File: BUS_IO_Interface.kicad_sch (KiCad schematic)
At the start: 21 parts, among them U13 AS1016204-0108X0PWAY, U28 MAX31331TETB+, U88 TCAN1044ADDFRQ1, Y26 32.768kHz

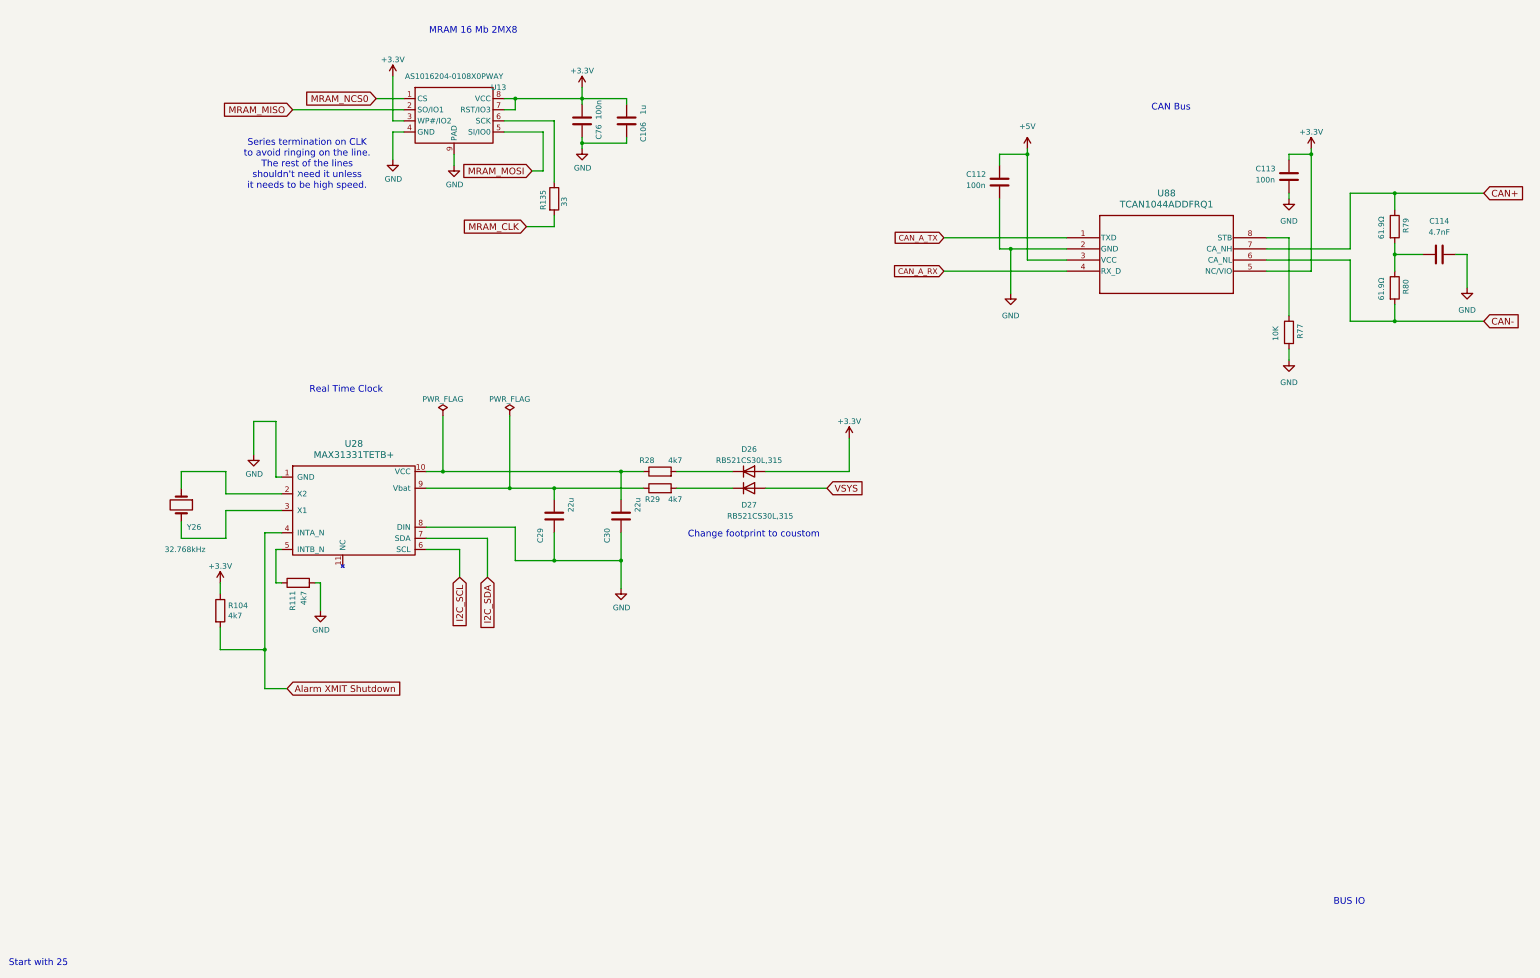
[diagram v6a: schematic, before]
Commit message: Re-annotate all parts
And get rid of the per-sheet annotation remarks.

Signed-off-by: Corey Minyard <corey@minyard.net>
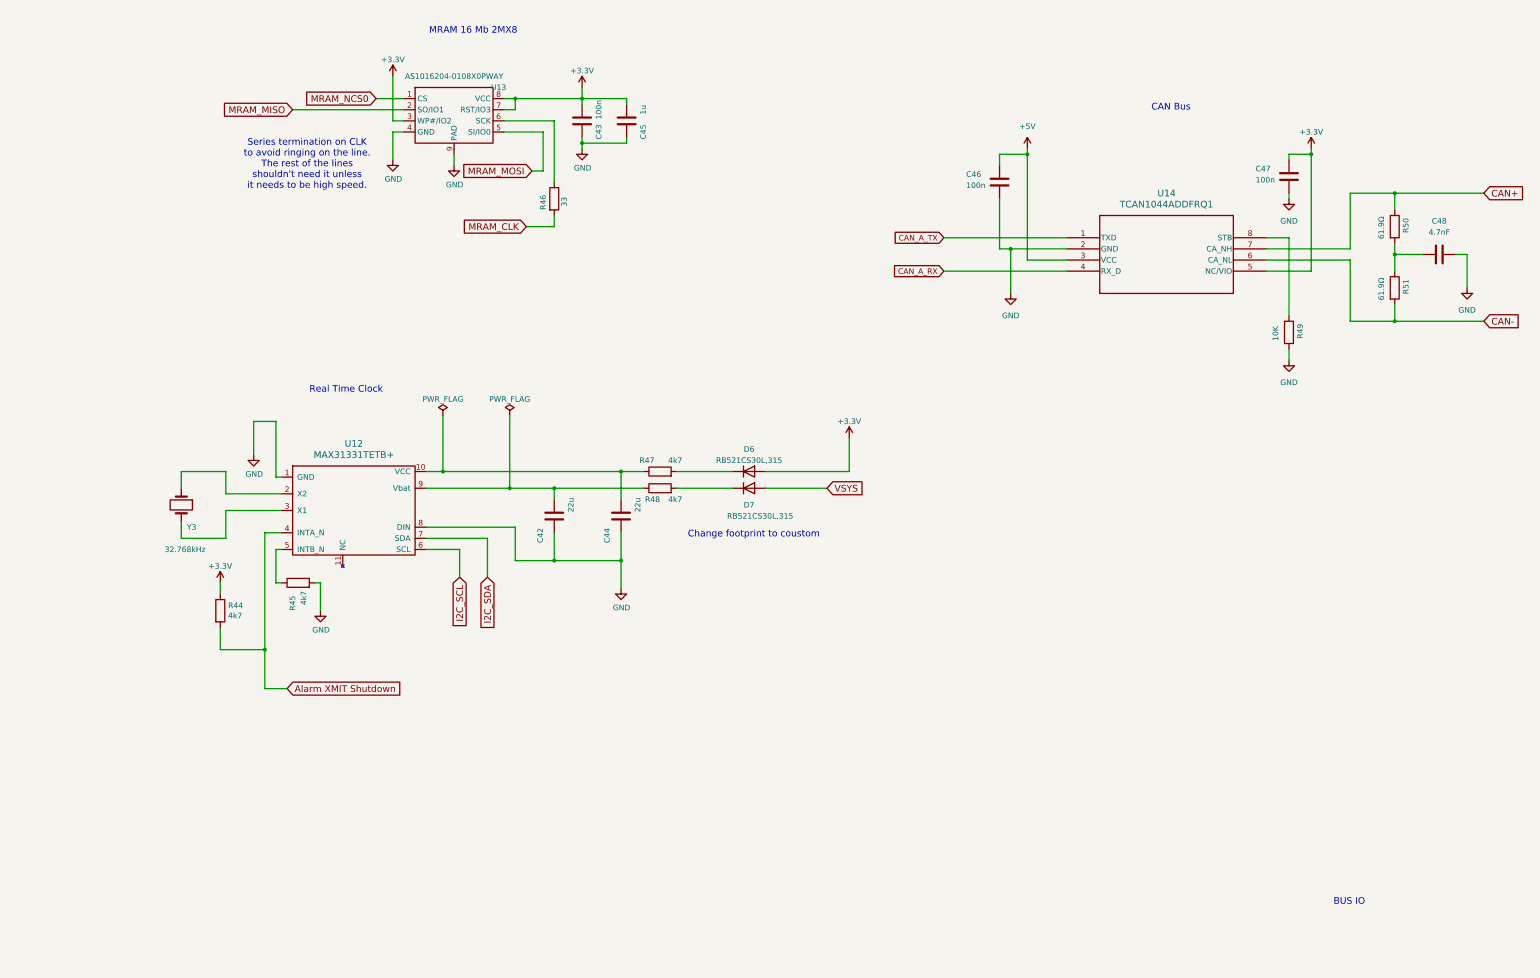
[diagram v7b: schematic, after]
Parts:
- renumbered C29 to C42, C76 to C43, C30 to C44, C106 to C45, C112 to C46, C113 to C47, C114 to C48, D26 to D6, D27 to D7, R104 to R44, R111 to R45, R135 to R46, R28 to R47, R29 to R48, R77 to R49, R79 to R50, R80 to R51, U28 to U12, U88 to U14, Y26 to Y3
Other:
- note removed: "Start with 25"

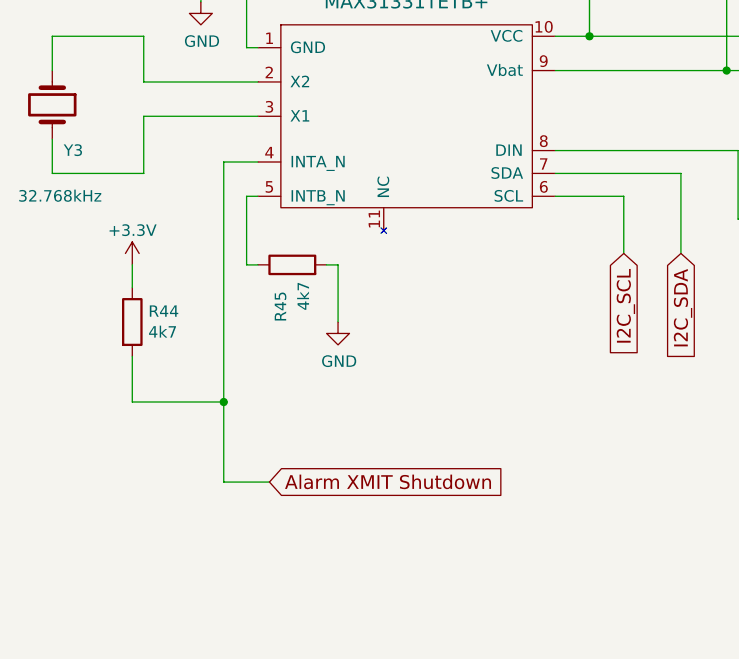
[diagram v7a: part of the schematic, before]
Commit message: Remove the PA watchdog
It wasn't doing anything useful.

Add an enable line from the processor to the TX AX5043.

Signed-off-by: Corey Minyard <corey@minyard.net>
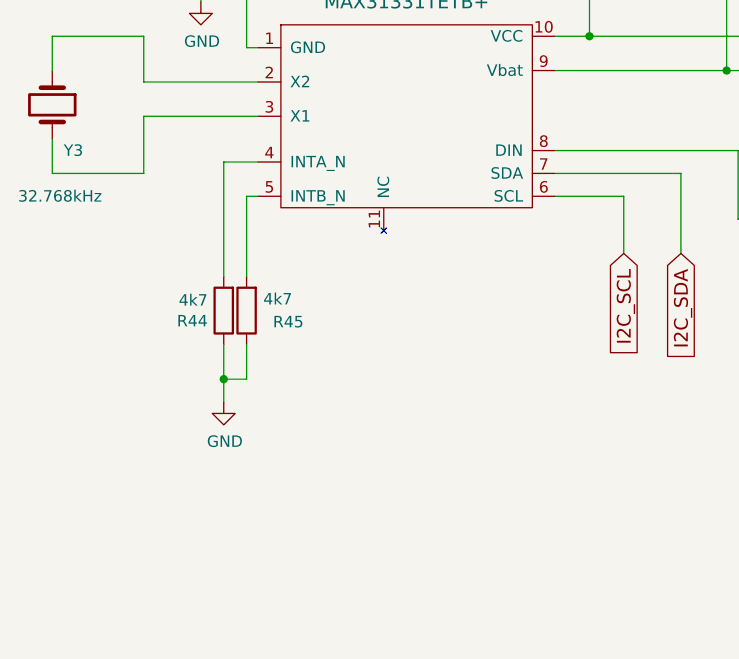
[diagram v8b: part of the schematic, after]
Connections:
- net +3.3V: no longer R44.1
- net GND: now also R44.1, R45.1; no longer R45.2
- net at U12.5 (INTB_N): now also R45.2; no longer R45.1
- net Alarm XMIT Shutdown: no longer names the net of R44.2, U12.4 (INTA_N)
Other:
- moved on the sheet: R44, R45
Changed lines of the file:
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@@
 	)
 	(junction
-		(at 90.17 186.69)
+		(at 90.17 184.15)
 		(diameter 0)
 		(color 0 0 0 0)
@@
 	(wire
 		(pts
-			(xy 328.93 73.66) (xy 328.93 100.33)
+			(xy 92.71 180.34) (xy 92.71 184.15)
 		)
 		(stroke
@@
 	(wire
 		(pts
-			(xy 90.17 186.69) (xy 90.17 195.58)
+			(xy 328.93 73.66) (xy 328.93 100.33)
 		)
 		(stroke
@@
 	(wire
 		(pts
-			(xy 90.17 160.02) (xy 90.17 186.69)
-		)
-		(stroke
-			(width 0)
-			(type default)
-		)
-	)
-	(wire
-		(pts
-			(xy 92.71 171.45) (xy 93.98 171.45)
+			(xy 90.17 160.02) (xy 90.17 172.72)
 		)
 		(stroke
@@
 	(wire
 		(pts
-			(xy 101.6 171.45) (xy 102.87 171.45)
-		)
-		(stroke
-			(width 0)
-			(type default)
-		)
-	)
-	(wire
-		(pts
 			(xy 257.81 83.82) (xy 257.81 95.25)
 		)
@@
 	(wire
 		(pts
-			(xy 80.01 181.61) (xy 80.01 186.69)
-		)
-		(stroke
-			(width 0)
-			(type default)
-		)
-	)
-	(wire
-		(pts
 			(xy 245.11 100.33) (xy 273.05 100.33)
 		)
@@
 	(wire
 		(pts
-			(xy 90.17 186.69) (xy 80.01 186.69)
+			(xy 153.67 68.58) (xy 153.67 77.47)
 		)
 		(stroke
@@
 	(wire
 		(pts
-			(xy 153.67 68.58) (xy 153.67 77.47)
+			(xy 147.32 63.5) (xy 147.32 60.96)
 		)
 		(stroke
@@
 	(wire
 		(pts
-			(xy 147.32 63.5) (xy 147.32 60.96)
+			(xy 146.05 149.86) (xy 156.21 149.86)
 		)
 		(stroke
@@
 	(wire
 		(pts
-			(xy 146.05 149.86) (xy 156.21 149.86)
+			(xy 156.21 149.86) (xy 176.53 149.86)
 		)
 		(stroke
@@
 	(wire
 		(pts
-			(xy 156.21 149.86) (xy 176.53 149.86)
+			(xy 156.21 149.86) (xy 156.21 152.4)
 		)
 		(stroke
@@
 	(wire
 		(pts
-			(xy 156.21 149.86) (xy 156.21 152.4)
+			(xy 364.49 96.52) (xy 364.49 104.14)
 		)
 		(stroke
@@
 	(wire
 		(pts
-			(xy 364.49 96.52) (xy 364.49 104.14)
+			(xy 90.17 180.34) (xy 90.17 184.15)
 		)
 		(stroke
@@
 	(wire
 		(pts
-			(xy 90.17 195.58) (xy 95.25 195.58)
+			(xy 328.93 72.39) (xy 328.93 73.66)
 		)
 		(stroke
@@
 	(wire
 		(pts
-			(xy 328.93 72.39) (xy 328.93 73.66)
+			(xy 90.17 184.15) (xy 90.17 186.69)
 		)
 		(stroke
@@
 	(wire
 		(pts
-			(xy 80.01 171.45) (xy 80.01 173.99)
-		)
-		(stroke
-			(width 0)
-			(type default)
-		)
-	)
-	(wire
-		(pts
 			(xy 81.28 154.94) (xy 81.28 161.29)
 		)
@@
 	(wire
 		(pts
-			(xy 92.71 163.83) (xy 92.71 171.45)
+			(xy 92.71 163.83) (xy 92.71 172.72)
 		)
 		(stroke
@@
 	(wire
 		(pts
-			(xy 102.87 171.45) (xy 102.87 177.8)
-		)
-		(stroke
-			(width 0)
-			(type default)
-		)
-	)
-	(wire
-		(pts
 			(xy 147.32 158.75) (xy 147.32 166.37)
 		)
@@
 	(wire
 		(pts
+			(xy 92.71 184.15) (xy 90.17 184.15)
+		)
+		(stroke
+			(width 0)
+			(type default)
+		)
+	)
+	(wire
+		(pts
 			(xy 71.12 157.48) (xy 71.12 161.29)
 		)
@@
 		)
 	)
-	(global_label "Alarm XMIT Shutdown"
-		(shape input)
-		(at 95.25 195.58 0)
-		(fields_autoplaced yes)
-		(effects
-			(font
-				(size 1.524 1.524)
-			)
-			(justify left)
-		)
-		(property "Intersheetrefs" "${INTERSHEET_REFS}"
-			(at 122.7212 195.58 0)
-			(effects
-				(font
-					(size 1.27 1.27)
-				)
-				(justify left)
-				(hide yes)
-			)
-		)
-	)
 	(symbol
 		(lib_id "Device:C")
@@
 	(symbol
 		(lib_id "Device:R")
-		(at 80.01 177.8 0)
+		(at 90.17 176.53 180)
 		(unit 1)
 		(exclude_from_sim no)
@@
 		(dnp no)
 		(property "Reference" "R44"
-			(at 81.788 176.6316 0)
+			(at 88.392 177.6984 0)
 			(effects
 				(font
@@
 		)
 		(property "Value" "4k7"
-			(at 81.788 178.943 0)
+			(at 88.392 175.387 0)
 			(effects
 				(font
@@
 		)
 		(property "Footprint" "Resistor_SMD:R_0603_1608Metric_Pad0.98x0.95mm_HandSolder"
-			(at 78.232 177.8 90)
+			(at 91.948 176.53 90)
 			(effects
 				(font
@@
 		)
 		(property "Datasheet" "~"
-			(at 80.01 177.8 0)
+			(at 90.17 176.53 0)
 			(effects
 				(font
 					(size 1.27 1.27)
 				)
+				(hide yes)
 			)
 		)
 		(property "Description" ""
-			(at 80.01 177.8 0)
+			(at 90.17 176.53 0)
 			(effects
 				(font
@@
 	)
 	(symbol
-		(lib_id "power:+3.3V")
-		(at 80.01 171.45 0)
-		(unit 1)
-		(exclude_from_sim no)
-		(in_bom yes)
-		(on_board yes)
-		(dnp no)
-		(fields_autoplaced yes)
-		(property "Reference" "#PWR0104"
-			(at 80.01 175.26 0)
-			(effects
-				(font
-					(size 1.27 1.27)
-				)
-				(hide yes)
-			)
-		)
-		(property "Value" "+3.3V"
-			(at 80.01 167.64 0)
-			(effects
-				(font
-					(size 1.27 1.27)
-				)
-			)
-		)
-		(property "Footprint" ""
-			(at 80.01 171.45 0)
-			(effects
-				(font
-					(size 1.27 1.27)
-				)
-				(hide yes)
-			)
-		)
-		(property "Datasheet" ""
-			(at 80.01 171.45 0)
-			(effects
-				(font
-					(size 1.27 1.27)
-				)
-				(hide yes)
-			)
-		)
-		(property "Description" ""
-			(at 80.01 171.45 0)
-			(effects
-				(font
-					(size 1.27 1.27)
-				)
-			)
-		)
-		(pin "1"
-		)
-		(instances
-			(project "PacSat_Dev_RevD_240614"
-				(path "/cc9f42d2-6985-41ac-acab-5ab7b01c5b38/aff81ec5-748c-4fc9-b1e8-df12a16f6289"
-					(reference "#PWR0104")
-					(unit 1)
-				)
-			)
-		)
-	)
-	(symbol
 		(lib_id "power:GND")
 		(at 260.35 105.41 0)
@@
 	(symbol
 		(lib_id "power:GND")
-		(at 102.87 177.8 0)
+		(at 90.17 186.69 0)
 		(unit 1)
 		(exclude_from_sim no)
@@
 		(dnp no)
 		(property "Reference" "#PWR0106"
-			(at 102.87 184.15 0)
+			(at 90.17 193.04 0)
 			(effects
 				(font
@@
 		)
 		(property "Value" "GND"
-			(at 102.997 182.1942 0)
+			(at 90.297 191.0842 0)
 			(effects
 				(font
@@
 		)
 		(property "Footprint" ""
-			(at 102.87 177.8 0)
+			(at 90.17 186.69 0)
 			(effects
 				(font
@@
 		)
 		(property "Datasheet" ""
-			(at 102.87 177.8 0)
+			(at 90.17 186.69 0)
 			(effects
 				(font
@@
 		)
 		(property "Description" ""
-			(at 102.87 177.8 0)
+			(at 90.17 186.69 0)
 			(effects
 				(font
@@
 		)
 		(instances
-			(project "PacSat_Dev_RevD_240614"
+			(project "PacSat_AFSK"
 				(path "/cc9f42d2-6985-41ac-acab-5ab7b01c5b38/aff81ec5-748c-4fc9-b1e8-df12a16f6289"
 					(reference "#PWR0106")
@@
 	(symbol
 		(lib_id "Device:R")
-		(at 97.79 171.45 90)
+		(at 92.71 176.53 180)
 		(unit 1)
 		(exclude_from_sim no)
@@
 		(dnp no)
 		(property "Reference" "R45"
-			(at 96.52 177.8 0)
+			(at 99.06 177.8 0)
 			(effects
 				(font
@@
 		)
 		(property "Value" "4k7"
-			(at 99.06 176.53 0)
+			(at 97.79 175.26 0)
 			(effects
 				(font
@@
 		)
 		(property "Footprint" "Resistor_SMD:R_0603_1608Metric_Pad0.98x0.95mm_HandSolder"
-			(at 97.79 173.228 90)
+			(at 94.488 176.53 90)
 			(effects
 				(font
@@
 		)
 		(property "Datasheet" "~"
-			(at 97.79 171.45 0)
+			(at 92.71 176.53 0)
 			(effects
 				(font
@@
 		)
 		(property "Description" ""
-			(at 97.79 171.45 0)
+			(at 92.71 176.53 0)
 			(effects
 				(font
